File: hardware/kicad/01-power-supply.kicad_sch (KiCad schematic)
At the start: 29 parts, among them J1 USB_C, J3 JST PH 2-pin, Q1 SI2301CDS, U2 IP5306, U3 SY8089AAAC, U4 USBLC6-2SC6

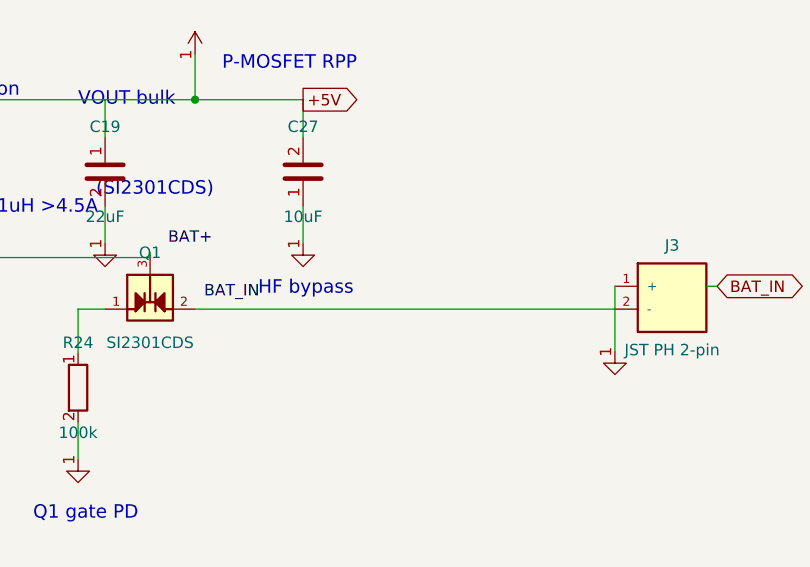
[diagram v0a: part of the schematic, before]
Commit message: sch+routing: EN is its own net, and the reset button was never in the netlist
Recovered in-flight work from a killed session; committed as-is so it can
be reviewed rather than lost. Measured, not asserted: the gate set goes
from 5 red of 6 to 3 red of 6.

SW_Push pins are HORIZONTAL (x +-5.08), not vertical like the R/C
symbols. Wiring the reset and boot buttons the way the passives are wired
put the wires BESIDE the pins: invisible in the plot, and the switches
never reached the netlist at all. That is why no gate had ever compared
them against the PCB.

Fixing the geometry alone would have wired SW_RST across +3V3 and GND,
because the schematic also tied EN straight to the 3V3 rail — so every
press of RESET would have been drawn as a dead short across the rail. The
PCB never had that: EN is its own copper there (T4: U1.3 sch='+3V3'
pcb='EN'). Only the drawing was wrong. EN now carries a global label so it
exports flat as "EN" and matches the PCB net name.

  verify_schematic_pin_connectivity  4 floating -> 0        PASS
  verify_dangling_copper             1 dead end -> 0        PASS
  verify_netlist_diff  T4            7 mismatches -> 1      still FAIL
  verify_net_class_widths            4 undersized -> 2      still FAIL

Two gate changes, both reported and neither suppressing: _LED_MAP is a
pin-vs-pad numbering translation with each side checked independently (a
wrong entry still fails T4), and _buried_in_own_pad exempts a track that
lies wholly inside a pad of its own net, using the pad's INSCRIBED circle
so rotation can never make it exempt more than it should.

Still open here: C3.1 sch='EN' pcb='+3V3' — the routing still ties the
reset cap to the rail.
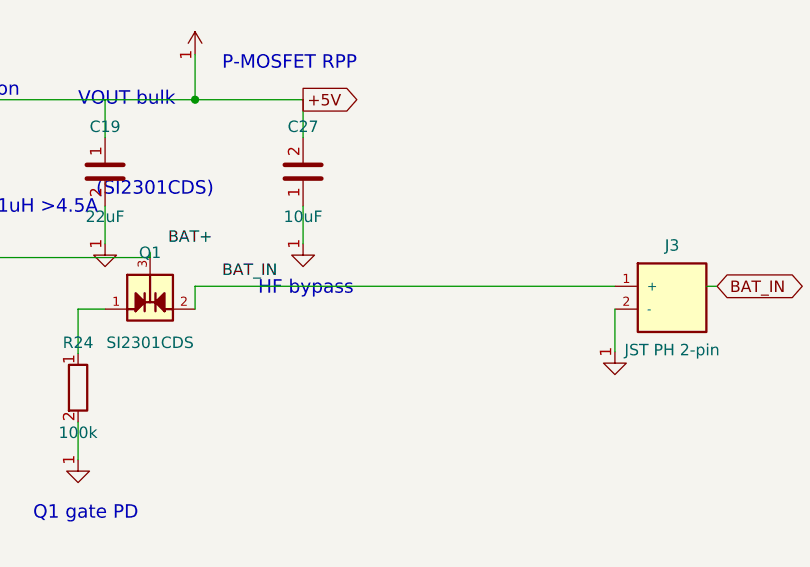
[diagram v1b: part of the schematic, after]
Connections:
- net GND: no longer J3.1 (+), Q1.2
- new net: J3.1 (+), Q1.2
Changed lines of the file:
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@@
   (wire (pts (xy 210 87.54) (xy 210 87)) (stroke (width 0) (type default)))
   (label "BAT+" (at 212 85.54 0) (effects (font (size 1.27 1.27))))
-  (wire (pts (xy 215 93.27) (xy 261.65 93.27)) (stroke (width 0) (type default)))
-  (wire (pts (xy 261.65 93.27) (xy 261.65 90.73)) (stroke (width 0) (type default)))
-  (label "BAT_IN" (at 216 91.5 0) (effects (font (size 1.27 1.27))))
+  (wire (pts (xy 215 93.27) (xy 215 90.73)) (stroke (width 0) (type default)))
+  (wire (pts (xy 215 90.73) (xy 261.65 90.73)) (stroke (width 0) (type default)))
+  (label "BAT_IN" (at 218 89.23 0) (effects (font (size 1.27 1.27))))
   (symbol (lib_id "R") (at 202 102 0) (unit 1) (exclude_from_sim no) (in_bom yes) (on_board yes) (dnp no) (property "Reference" "R24" (at 202 97.0 0) (effects (font (size 1.27 1.27)))) (property "Value" "100k" (at 202 107.0 0) (effects (font (size 1.27 1.27)))) (pin "1") (pin "2") (instances (project "esp32-emu-turbo" (path "/00000002-cafe-4000-8000-000000000002" (reference "R24") (unit 1)))))
   (text "Q1 gate PD" (at 197 116 0) (effects (font (size 1.5 1.5)) (justify left)))
